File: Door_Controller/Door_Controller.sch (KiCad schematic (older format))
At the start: 0 parts

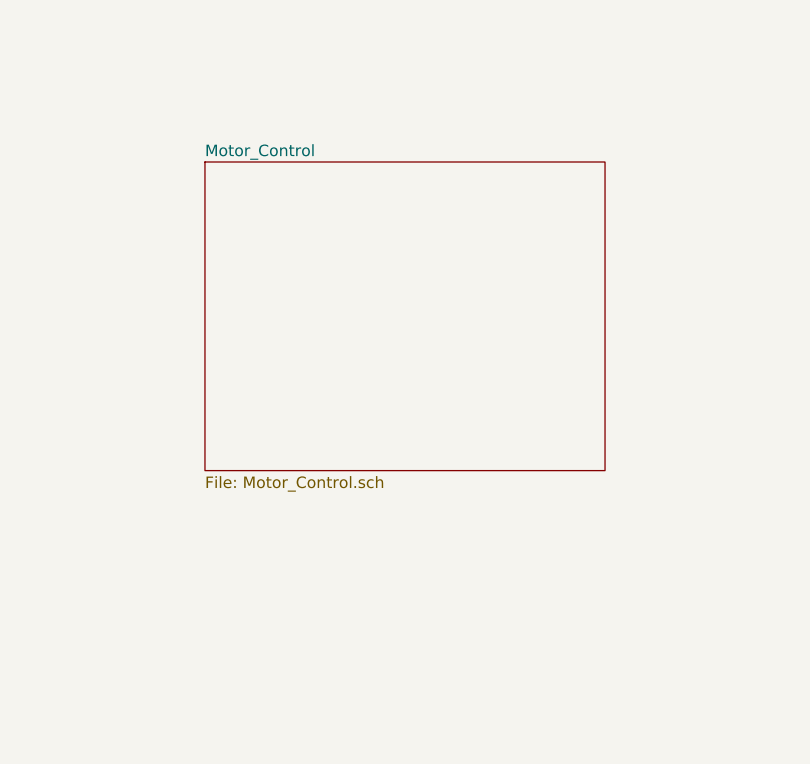
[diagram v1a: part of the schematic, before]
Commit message: update motor control pins
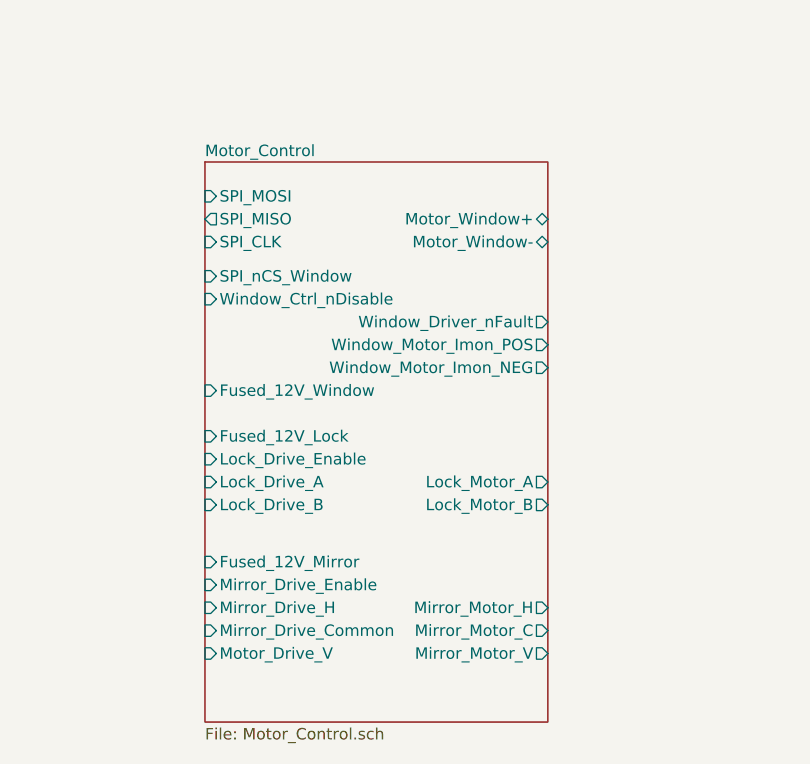
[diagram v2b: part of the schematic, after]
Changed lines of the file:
@@
 $Descr A4 11693 8268
 encoding utf-8
-Sheet 1 8
+Sheet 1 12
 Title "Door Controller - Top Level"
 Date "2020-11-12"
@@
 $EndSheet
 $Sheet
-S 2500 4150 1750 1350
+S 2500 4150 1500 2450
 U 5FB4C28C
 F0 "Motor_Control" 50
 F1 "Motor_Control.sch" 50
+F2 "SPI_MOSI" I L 2500 4300 50
+F3 "SPI_CLK" I L 2500 4500 50
+F4 "SPI_MISO" O L 2500 4400 50
+F5 "SPI_nCS_Window" I L 2500 4650 50
+F6 "Motor_Window+" B R 4000 4400 50
+F7 "Window_Driver_nFault" O R 4000 4850 50
+F8 "Window_Ctrl_nDisable" I L 2500 4750 50
+F9 "Window_Motor_Imon_POS" O R 4000 4950 50
+F10 "Window_Motor_Imon_NEG" O R 4000 5050 50
+F11 "Motor_Window-" B R 4000 4500 50
+F12 "Fused_12V_Window" I L 2500 5150 50
+F13 "Lock_Drive_B" I L 2500 5650 50
+F14 "Lock_Motor_A" O R 4000 5550 50
+F15 "Lock_Motor_B" O R 4000 5650 50
+F16 "Lock_Drive_A" I L 2500 5550 50
+F17 "Lock_Drive_Enable" I L 2500 5450 50
+F18 "Fused_12V_Lock" I L 2500 5350 50
+F19 "Mirror_Drive_Enable" I L 2500 6000 50
+F20 "Fused_12V_Mirror" I L 2500 5900 50
+F21 "Mirror_Motor_H" O R 4000 6100 50
+F22 "Mirror_Drive_H" I L 2500 6100 50
+F23 "Mirror_Motor_C" O R 4000 6200 50
+F24 "Mirror_Drive_Common" I L 2500 6200 50
+F25 "Mirror_Motor_V" O R 4000 6300 50
+F26 "Motor_Drive_V" I L 2500 6300 50
 $EndSheet
 $EndSCHEMATC
